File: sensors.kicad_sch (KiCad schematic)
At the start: 3 parts, among them IC5 BME690, U2 BME280, U3 BMP581

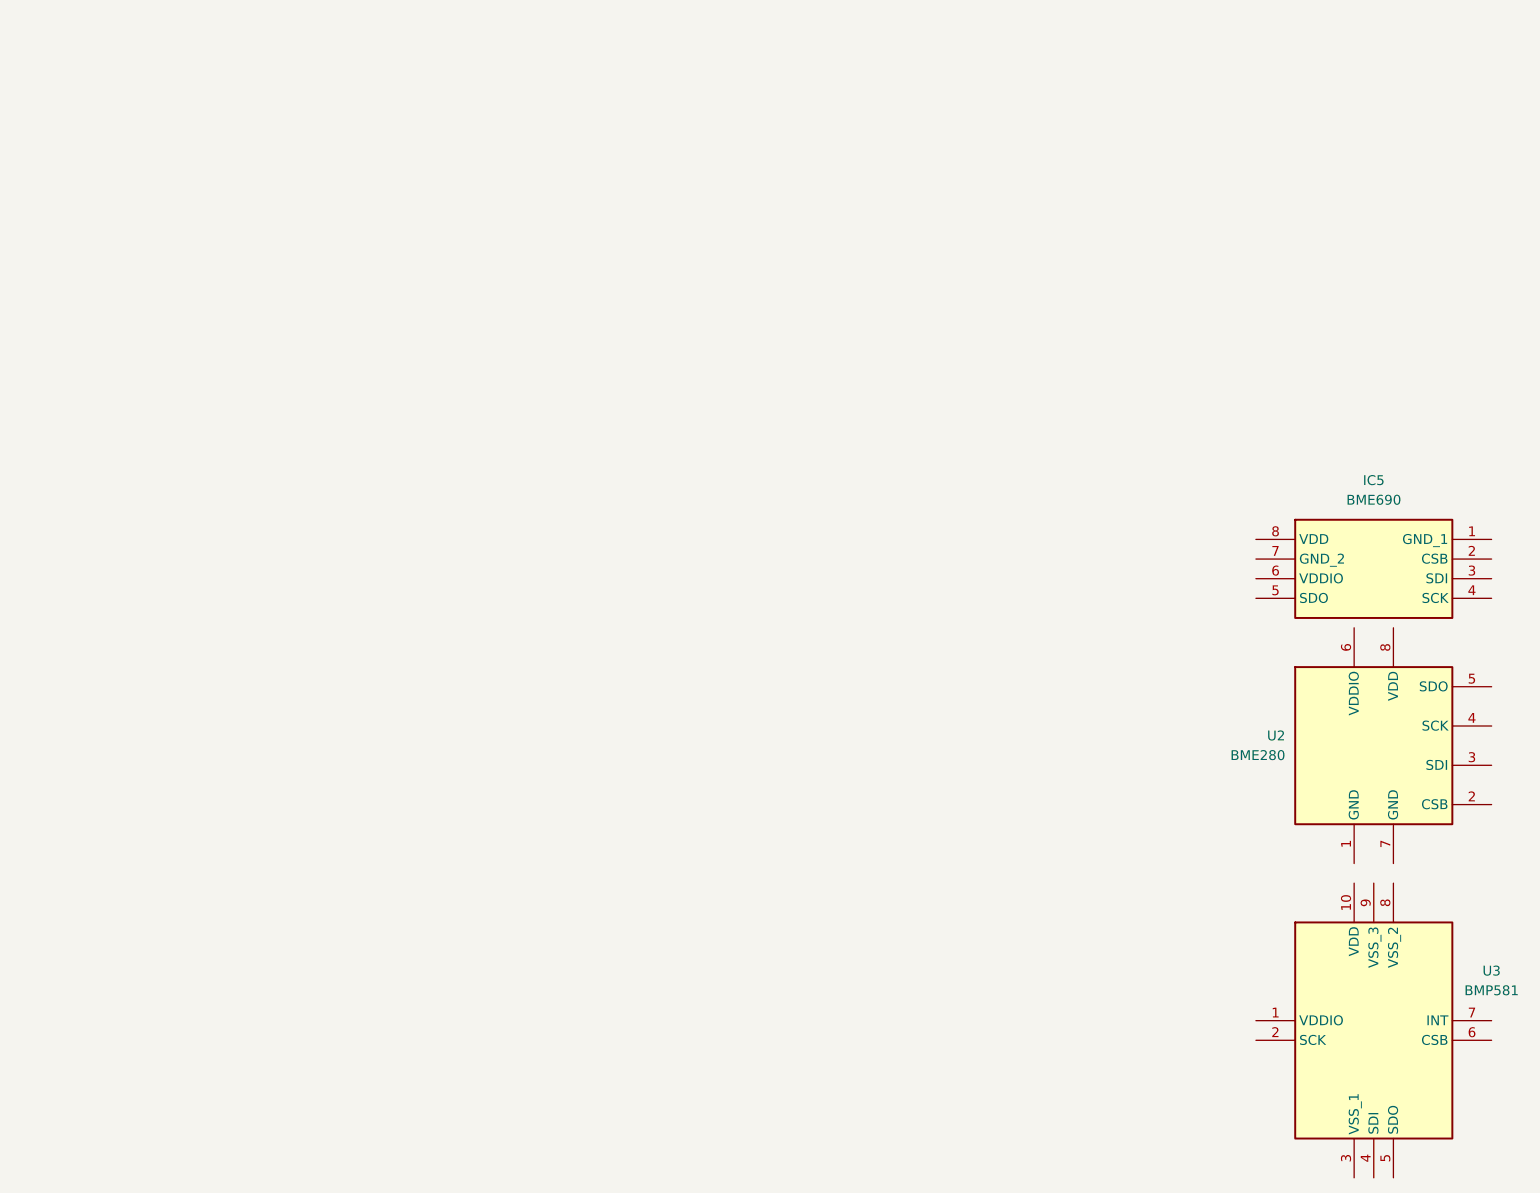
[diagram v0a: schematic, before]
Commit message: Add block diagram in a sheet
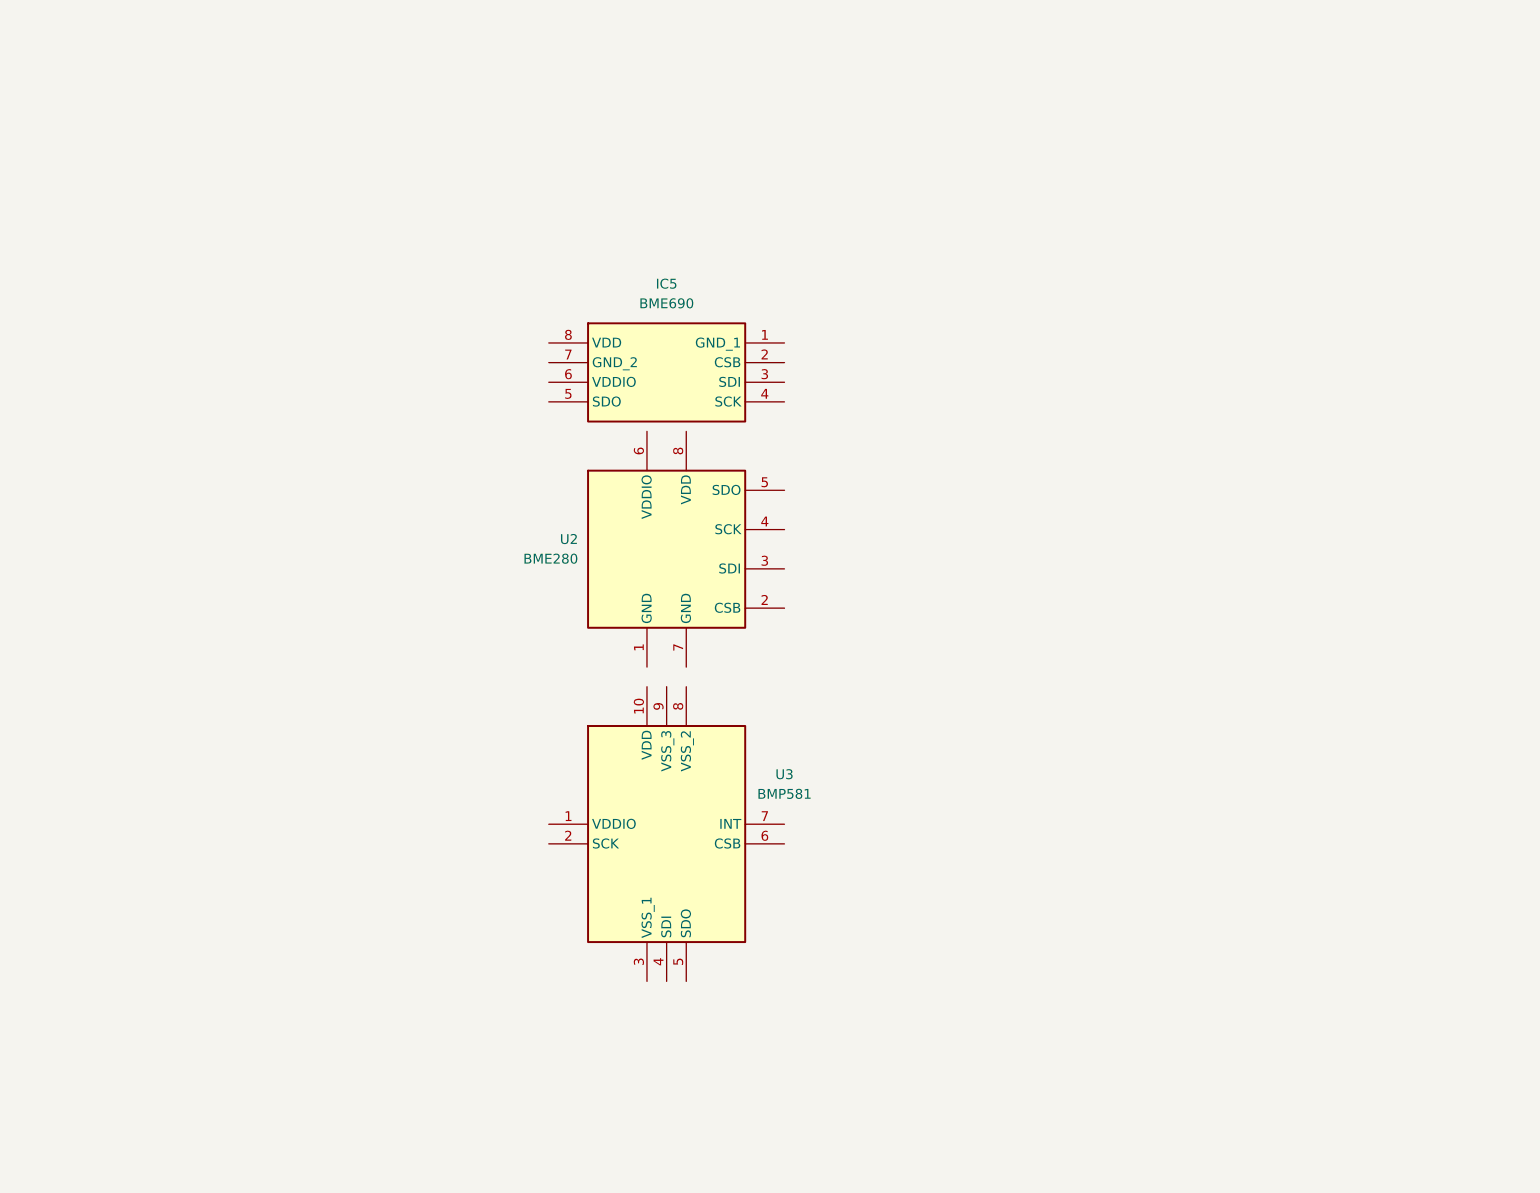
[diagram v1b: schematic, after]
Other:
- moved on the sheet: IC5, U2, U3
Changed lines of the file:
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@@
 	(generator "eeschema")
 	(generator_version "9.0")
-	(paper "A3")
+	(paper "A4")
 	(title_block
 		(date "2025-11-01")
@@
 	(symbol
 		(lib_id "weather-station-poc-sym:BMP581")
-		(at 219.71 146.05 0)
+		(at 128.27 120.65 0)
 		(unit 1)
 		(exclude_from_sim no)
@@
 		(fields_autoplaced yes)
 		(property "Reference" "U3"
-			(at 250.19 139.6298 0)
+			(at 158.75 114.2298 0)
 			(effects
 				(font
@@
 		)
 		(property "Value" "BMP581"
-			(at 250.19 142.1698 0)
+			(at 158.75 116.7698 0)
 			(effects
 				(font
@@
 		)
 		(property "Footprint" "BMP581"
-			(at 246.38 230.81 0)
+			(at 154.94 205.41 0)
 			(effects
 				(font
@@
 		)
 		(property "Datasheet" "https://www.bosch-sensortec.com/media/boschsensortec/downloads/datasheets/bst-bmp581-ds004.pdf"
-			(at 246.38 330.81 0)
+			(at 154.94 305.41 0)
 			(effects
 				(font
@@
 		)
 		(property "Description" "Pressure Sensor 4.35PSI ~ 18.13PSI (30kPa ~ 125kPa) Absolute 10-WFLGA"
-			(at 219.71 146.05 0)
+			(at 128.27 120.65 0)
 			(effects
 				(font
@@
 		)
 		(property "Height" "0.8"
-			(at 246.38 530.81 0)
+			(at 154.94 505.41 0)
 			(effects
 				(font
@@
 		)
 		(property "Mouser Part Number" "262-BMP581"
-			(at 246.38 630.81 0)
+			(at 154.94 605.41 0)
 			(effects
 				(font
@@
 		)
 		(property "Mouser Price/Stock" "https://www.mouser.co.uk/ProductDetail/Bosch-Sensortec/BMP581?qs=Li%252BoUPsLEntPL9tlFmcgXg%3D%3D"
-			(at 246.38 730.81 0)
+			(at 154.94 705.41 0)
 			(effects
 				(font
@@
 		)
 		(property "Manufacturer_Name" "BOSCH"
-			(at 246.38 830.81 0)
+			(at 154.94 805.41 0)
 			(effects
 				(font
@@
 		)
 		(property "Manufacturer_Part_Number" "BMP581"
-			(at 246.38 930.81 0)
+			(at 154.94 905.41 0)
 			(effects
 				(font
@@
 	(symbol
 		(lib_id "Sensor:BME280")
-		(at 234.95 110.49 0)
+		(at 143.51 85.09 0)
 		(unit 1)
 		(exclude_from_sim no)
@@
 		(fields_autoplaced yes)
 		(property "Reference" "U2"
-			(at 223.52 109.2199 0)
+			(at 132.08 83.8199 0)
 			(effects
 				(font
@@
 		)
 		(property "Value" "BME280"
-			(at 223.52 111.7599 0)
+			(at 132.08 86.3599 0)
 			(effects
 				(font
@@
 		)
 		(property "Footprint" "Package_LGA:Bosch_LGA-8_2.5x2.5mm_P0.65mm_ClockwisePinNumbering"
-			(at 273.05 121.92 0)
+			(at 181.61 96.52 0)
 			(effects
 				(font
@@
 		)
 		(property "Datasheet" "https://www.bosch-sensortec.com/media/boschsensortec/downloads/datasheets/bst-bme280-ds002.pdf"
-			(at 234.95 115.57 0)
+			(at 143.51 90.17 0)
 			(effects
 				(font
@@
 		)
 		(property "Description" "3-in-1 sensor, humidity, pressure, temperature, I2C and SPI interface, 1.71-3.6V, LGA-8"
-			(at 234.95 110.49 0)
+			(at 143.51 85.09 0)
 			(effects
 				(font
@@
 	(symbol
 		(lib_id "weather-station-poc-sym:BME690")
-		(at 219.71 83.82 0)
+		(at 128.27 58.42 0)
 		(unit 1)
 		(exclude_from_sim no)
@@
 		(fields_autoplaced yes)
 		(property "Reference" "IC5"
-			(at 234.95 76.2 0)
+			(at 143.51 50.8 0)
 			(effects
 				(font
@@
 		)
 		(property "Value" "BME690"
-			(at 234.95 78.74 0)
+			(at 143.51 53.34 0)
 			(effects
 				(font
@@
 		)
 		(property "Footprint" "BME690"
-			(at 246.38 178.74 0)
+			(at 154.94 153.34 0)
 			(effects
 				(font
@@
 		)
 		(property "Datasheet" "https://www.bosch-sensortec.com/products/environmental-sensors/gas-sensors/bme690/#documents"
-			(at 246.38 278.74 0)
+			(at 154.94 253.34 0)
 			(effects
 				(font
@@
 		)
 		(property "Description" "Multiple Function Sensor Modules BME690 is the gas sensor with Artificial Intelligence (AI) and integrated high-linearity and high-accuracy  pressure, humidity and temperature sensors."
-			(at 219.71 83.82 0)
+			(at 128.27 58.42 0)
 			(effects
 				(font
@@
 		)
 		(property "Height" "1"
-			(at 246.38 478.74 0)
+			(at 154.94 453.34 0)
 			(effects
 				(font
@@
 		)
 		(property "Mouser Part Number" "262-BME690"
-			(at 246.38 578.74 0)
+			(at 154.94 553.34 0)
 			(effects
 				(font
@@
 		)
 		(property "Mouser Price/Stock" "https://www.mouser.co.uk/ProductDetail/Bosch-Sensortec/BME690?qs=%252BXxaIXUDbq38jwlEAGDF7A%3D%3D"
-			(at 246.38 678.74 0)
+			(at 154.94 653.34 0)
 			(effects
 				(font
@@
 		)
 		(property "Manufacturer_Name" "BOSCH"
-			(at 246.38 778.74 0)
+			(at 154.94 753.34 0)
 			(effects
 				(font
@@
 		)
 		(property "Manufacturer_Part_Number" "BME690"
-			(at 246.38 878.74 0)
-			(effects
-				(font
+			(at 154.94 853.34 0)
+			(effects
+				(font

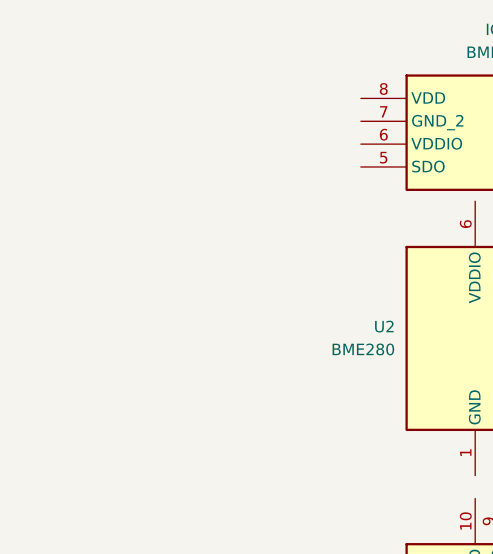
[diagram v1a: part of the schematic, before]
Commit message: Beginning of all signals definition
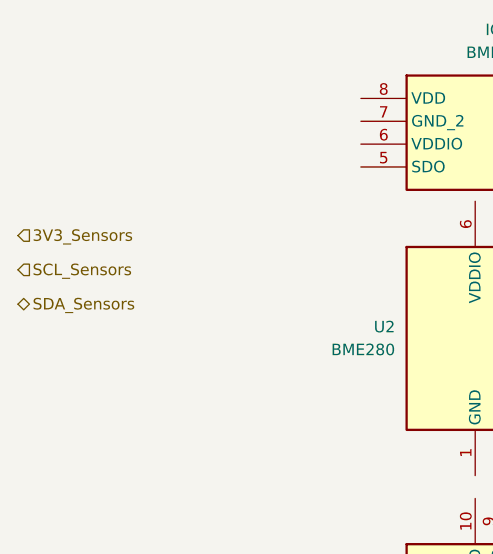
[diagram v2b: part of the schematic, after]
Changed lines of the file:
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@@
 		(date "2025-11-01")
+	)
+	(hierarchical_label "3V3_Sensors"
+		(shape input)
+		(at 90.17 73.66 0)
+		(effects
+			(font
+				(size 1.27 1.27)
+			)
+			(justify left)
+		)
+	)
+	(hierarchical_label "SCL_Sensors"
+		(shape input)
+		(at 90.17 77.47 0)
+		(effects
+			(font
+				(size 1.27 1.27)
+			)
+			(justify left)
+		)
+	)
+	(hierarchical_label "SDA_Sensors"
+		(shape bidirectional)
+		(at 90.17 81.28 0)
+		(effects
+			(font
+				(size 1.27 1.27)
+			)
+			(justify left)
+		)
 	)
 	(symbol

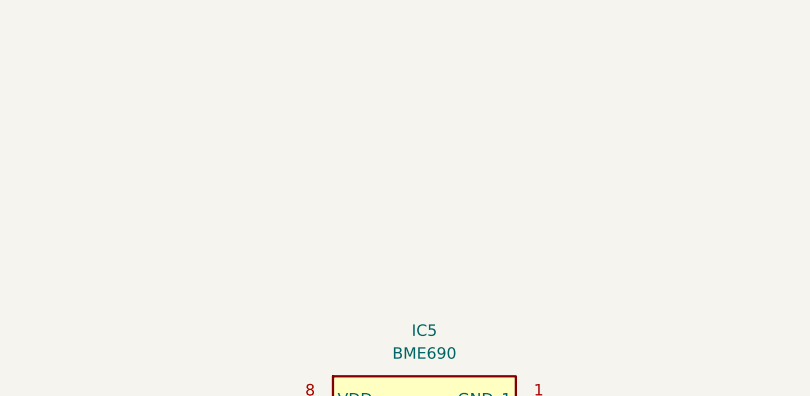
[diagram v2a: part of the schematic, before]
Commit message: Use local labels for RGB bus in folio and add title for all folio
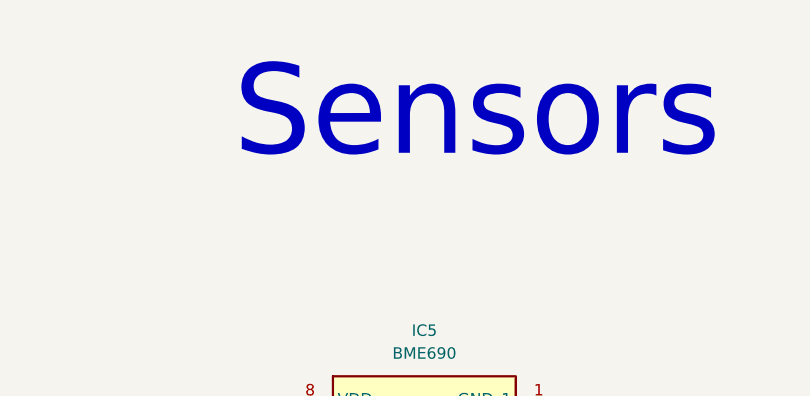
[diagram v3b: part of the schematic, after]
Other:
- note added: "Sensors"
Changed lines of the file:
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@@
 		(date "2025-11-01")
+	)
+	(text "Sensors"
+		(exclude_from_sim no)
+		(at 149.352 26.67 0)
+		(effects
+			(font
+				(size 10 10)
+			)
+		)
 	)
 	(hierarchical_label "3V3_Sensors"
